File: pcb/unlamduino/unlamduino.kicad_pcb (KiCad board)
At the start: 2 copper layers, 41 parts, among them IC2 ATMEGA328-P, P3 CONN_01X08, U1 LM2576, U2 AP111733, Y2 16MHz

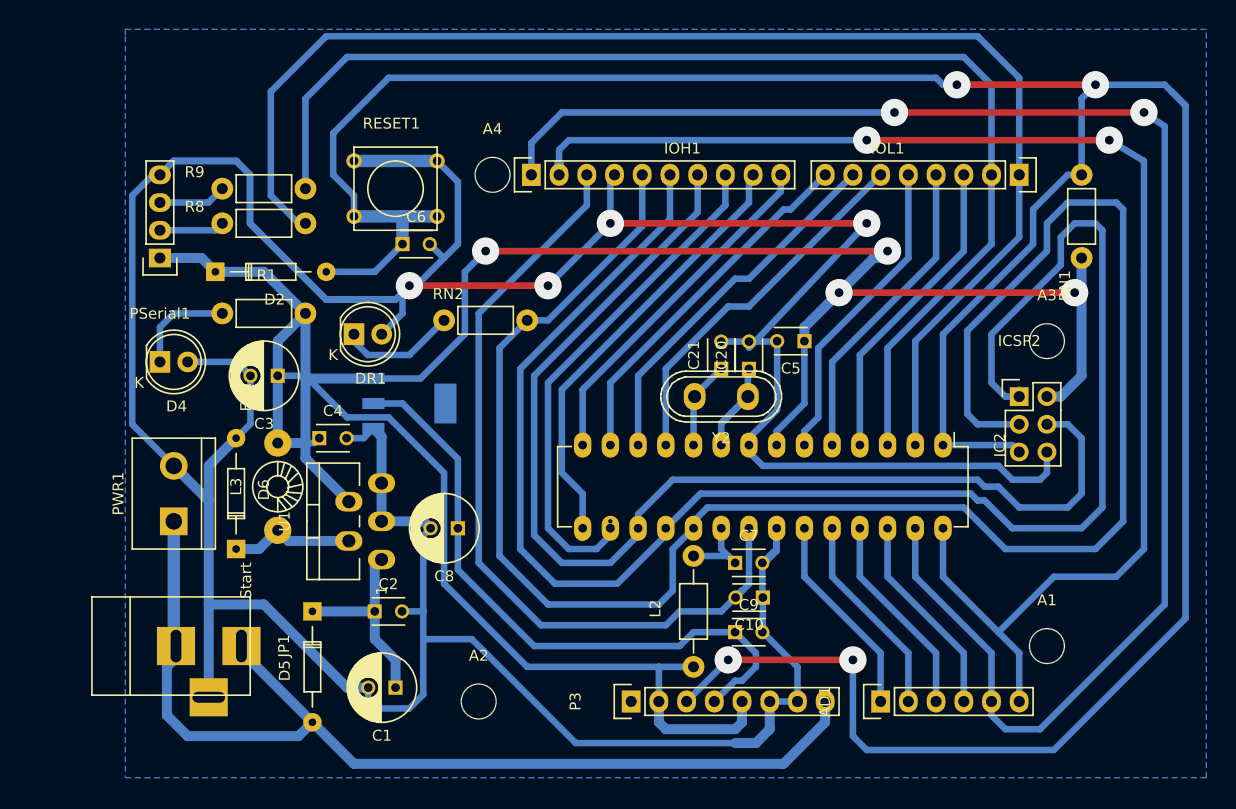
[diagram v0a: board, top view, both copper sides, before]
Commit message: Dibujo del borde de la placa.
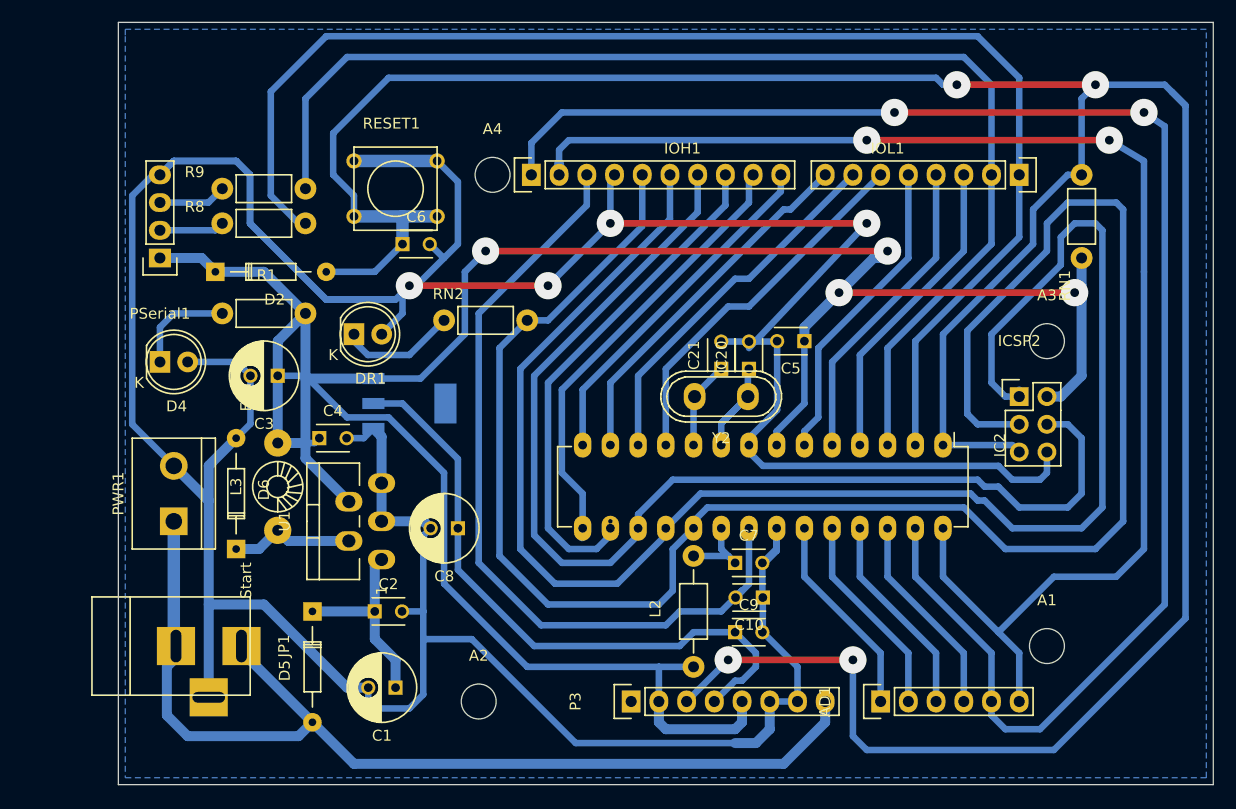
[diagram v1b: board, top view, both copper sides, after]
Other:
- board outline added: 100.3 x 69.8 mm
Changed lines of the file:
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@@
     (area 0 0 0 0)
     (thickness 1.6)
-    (drawings 2)
+    (drawings 6)
     (tracks 477)
     (zones 0)
@@
     (pad 1 np_thru_hole circle (at 0 0) (size 3.2 3.2) (drill 3.2) (layers *.Cu *.Mask F.SilkS))
   )
+  (gr_line (start 158.115 38.735) (end 158.115 108.585) (angle 90) (layer Edge.Cuts) (width 0.1))
+  (gr_line (start 258.445 38.735) (end 158.115 38.735) (angle 90) (layer Edge.Cuts) (width 0.1))
+  (gr_line (start 258.445 108.585) (end 258.445 38.735) (angle 90) (layer Edge.Cuts) (width 0.1))
+  (gr_line (start 158.115 108.585) (end 258.445 108.585) (angle 90) (layer Edge.Cuts) (width 0.1))
   (dimension 72 (width 0.3) (layer Cmts.User)
     (gr_text 72,000mm (at 142.65 76 270) (layer Cmts.User)

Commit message: Agregado de texto indicador de Montajes y diseño. Patas 1 de los integrados
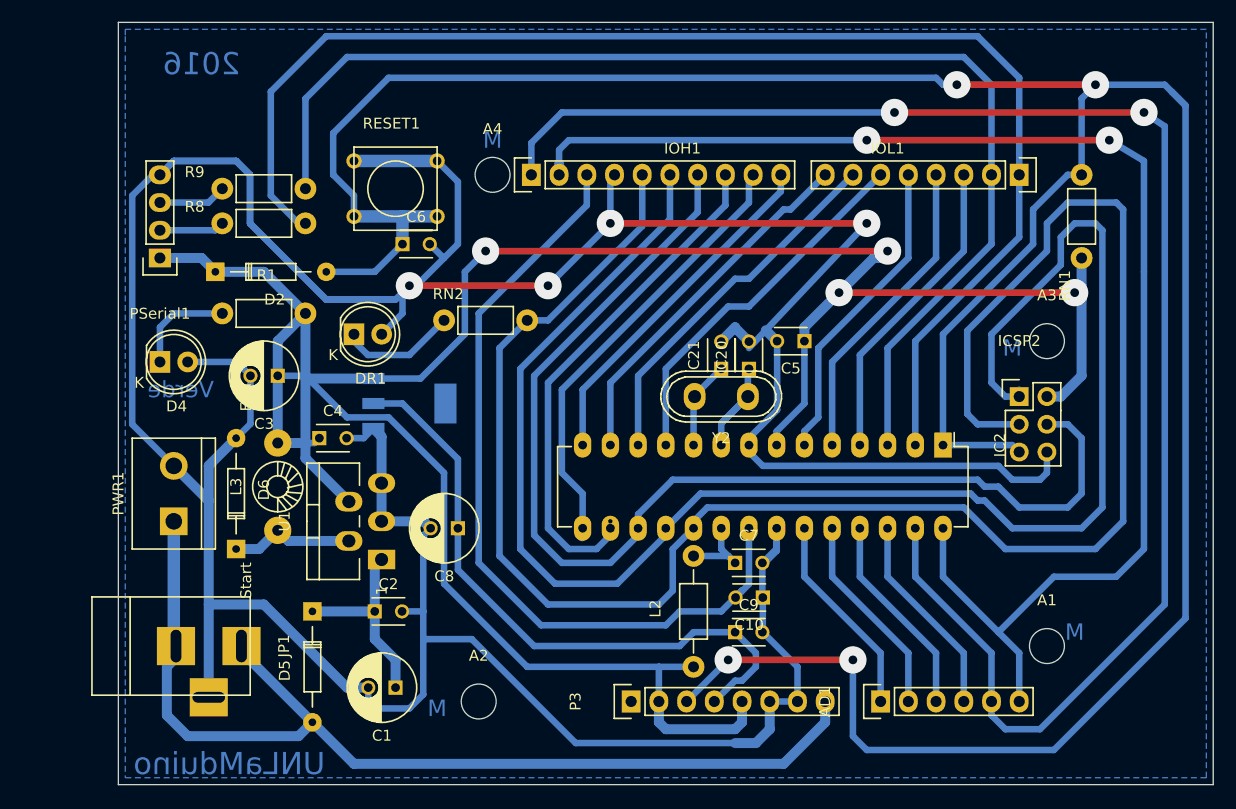
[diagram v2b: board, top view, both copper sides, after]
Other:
- board text added: "2016"
- board text added: "M"
- board text added: "UNLaMduino"
- board text added: "Verde"
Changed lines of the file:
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@@
     (links 101)
     (no_connects 0)
-    (area 0 0 0 0)
+    (area 136.57143 38.684999 264.000001 128.700001)
     (thickness 1.6)
-    (drawings 6)
-    (tracks 477)
+    (drawings 13)
+    (tracks 482)
     (zones 0)
     (modules 41)
@@
     (pad 3 thru_hole oval (at 0 3.79984 180) (size 2.49936 1.80086) (drill 1.19888) (layers *.Cu *.Mask F.SilkS)
       (net 7 GND))
-    (pad 1 thru_hole oval (at -3.50012 3.79984 180) (size 2.49936 1.80086) (drill 1.19888) (layers *.Cu *.Mask F.SilkS)
+    (pad 1 thru_hole rect (at -3.50012 3.79984 180) (size 2.49936 1.80086) (drill 1.19888) (layers *.Cu *.Mask F.SilkS)
       (net 8 "Net-(C1-Pad1)"))
     (pad 5 thru_hole oval (at 3.50012 3.79984 180) (size 2.49936 1.80086) (drill 1.19888) (layers *.Cu *.Mask F.SilkS)
@@
     (fp_line (start 0.135 35.315) (end 7.485 35.315) (layer F.SilkS) (width 0.15))
     (fp_line (start 0.135 -1.025) (end -1.15 -1.025) (layer F.SilkS) (width 0.15))
-    (pad 1 thru_hole oval (at 0 0 270) (size 2.3 1.6) (drill 0.8) (layers *.Cu *.Mask F.SilkS)
+    (pad 1 thru_hole rect (at 0 0 270) (size 2.3 1.6) (drill 0.8) (layers *.Cu *.Mask F.SilkS)
       (net 10 /RESET))
     (pad 2 thru_hole oval (at 0 2.54 270) (size 2.3 1.6) (drill 0.8) (layers *.Cu *.Mask F.SilkS)
@@
     (pad 1 np_thru_hole circle (at 0 0) (size 3.2 3.2) (drill 3.2) (layers *.Cu *.Mask F.SilkS))
   )
+  (gr_text "2016\n" (at 165.735 42.545) (layer B.Cu)
+    (effects (font (size 2.032 2.032) (thickness 0.381)) (justify mirror))
+  )
+  (gr_text UNLaMduino (at 168.275 106.68) (layer B.Cu)
+    (effects (font (size 2.032 2.032) (thickness 0.3556)) (justify mirror))
+  )
+  (gr_text Verde (at 163.83 72.39) (layer B.Cu)
+    (effects (font (size 1.5 1.5) (thickness 0.3)) (justify mirror))
+  )
+  (gr_text M (at 187.325 101.6) (layer B.Cu)
+    (effects (font (size 1.5 1.5) (thickness 0.3)) (justify mirror))
+  )
+  (gr_text M (at 192.405 49.53) (layer B.Cu)
+    (effects (font (size 1.5 1.5) (thickness 0.3)) (justify mirror))
+  )
+  (gr_text M (at 240.03 68.58) (layer B.Cu)
+    (effects (font (size 1.5 1.5) (thickness 0.3)) (justify mirror))
+  )
+  (gr_text M (at 245.745 94.615) (layer B.Cu)
+    (effects (font (size 1.5 1.5) (thickness 0.3)) (justify mirror))
+  )
   (gr_line (start 158.115 38.735) (end 158.115 108.585) (angle 90) (layer Edge.Cuts) (width 0.1))
   (gr_line (start 258.445 38.735) (end 158.115 38.735) (angle 90) (layer Edge.Cuts) (width 0.1))
@@
   (segment (start 238.76 94.615) (end 240.665 96.52) (width 0.6) (layer B.Cu) (net 6))
   (segment (start 198.501 52.705) (end 198.501 51.689) (width 0.9144) (layer B.Cu) (net 6) (status 30))
+  (segment (start 218.48 67.945) (end 218.44 67.945) (width 0.9144) (layer B.Cu) (net 7))
+  (segment (start 218.44 67.945) (end 217.442143 66.947143) (width 0.9144) (layer B.Cu) (net 7))
+  (segment (start 213.36 67.985) (end 213.36 67.945) (width 0.9144) (layer B.Cu) (net 7))
+  (segment (start 213.36 67.945) (end 214.63 66.675) (width 0.9144) (layer B.Cu) (net 7))
+  (segment (start 214.63 66.715) (end 215.9 67.985) (width 0.9144) (layer B.Cu) (net 7))
+  (segment (start 214.63 66.675) (end 214.63 66.715) (width 0.9144) (layer B.Cu) (net 7))
   (segment (start 182.23484 84.455) (end 186.095 84.455) (width 0.9144) (layer B.Cu) (net 7) (status 10))
   (segment (start 186.095 84.455) (end 186.73 85.09) (width 0.9144) (layer B.Cu) (net 7) (status 20))
@@
   (segment (start 240.03 80.645) (end 242.57 80.645) (width 0.6) (layer B.Cu) (net 7))
   (segment (start 238.76 79.375) (end 240.03 80.645) (width 0.6) (layer B.Cu) (net 7))
-  (segment (start 215.9 67.985) (end 218.44 67.985) (width 0.6) (layer B.Cu) (net 7) (status 30))
   (segment (start 218.44 67.985) (end 218.48 67.945) (width 0.6) (layer B.Cu) (net 7) (status 30))
-  (segment (start 213.36 67.985) (end 215.9 67.985) (width 0.6) (layer B.Cu) (net 7) (status 30))
   (segment (start 181.015 99.695) (end 181.015 101.005) (width 0.6) (layer B.Cu) (net 7) (status 10))
   (segment (start 184.785 101.6) (end 186.055 100.33) (width 0.6) (layer B.Cu) (net 7))
@@
   (segment (start 217.335002 88.265) (end 217.13 88.265) (width 0.6) (layer B.Cu) (net 7) (status 30))
   (segment (start 217.805 100.965) (end 217.805 101.6) (width 0.6) (layer B.Cu) (net 7) (status 30))
-  (segment (start 215.9 68.58) (end 226.695 57.15) (width 0.6) (layer B.Cu) (net 7) (status 10))
+  (segment (start 215.9 68.58) (end 217.442143 66.947143) (width 0.6) (layer B.Cu) (net 7) (status 10))
+  (segment (start 217.442143 66.947143) (end 226.695 57.15) (width 0.6) (layer B.Cu) (net 7) (status 10))
   (segment (start 203.2 57.15) (end 203.2 53.086) (width 0.6) (layer B.Cu) (net 7) (status 20))
   (via (at 203.2 57.15) (size 2.5) (drill 0.8) (layers F.Cu B.Cu) (net 7))

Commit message: Acomodado de serigrafía
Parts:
- moved IOH1 22.9 mm to (218.8, 52.7), turned to 270 degrees
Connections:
- IOH1 pad 1: /AD4/SDA -> /IO8
- IOH1 pad 10: /IO8 -> /AD4/SDA
- IOH1 pad 2: /AD5/SCL -> /IO9
- IOH1 pad 3: /AREF -> /IO10
- IOH1 pad 4: GND -> /IO11
- IOH1 pad 5: /IO13 -> /IO12
- IOH1 pad 6: /IO12 -> /IO13
- IOH1 pad 7: /IO11 -> GND
- IOH1 pad 8: /IO10 -> /AREF
- IOH1 pad 9: /IO9 -> /AD5/SCL
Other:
- board text added: "0"
- board text added: "Analog"

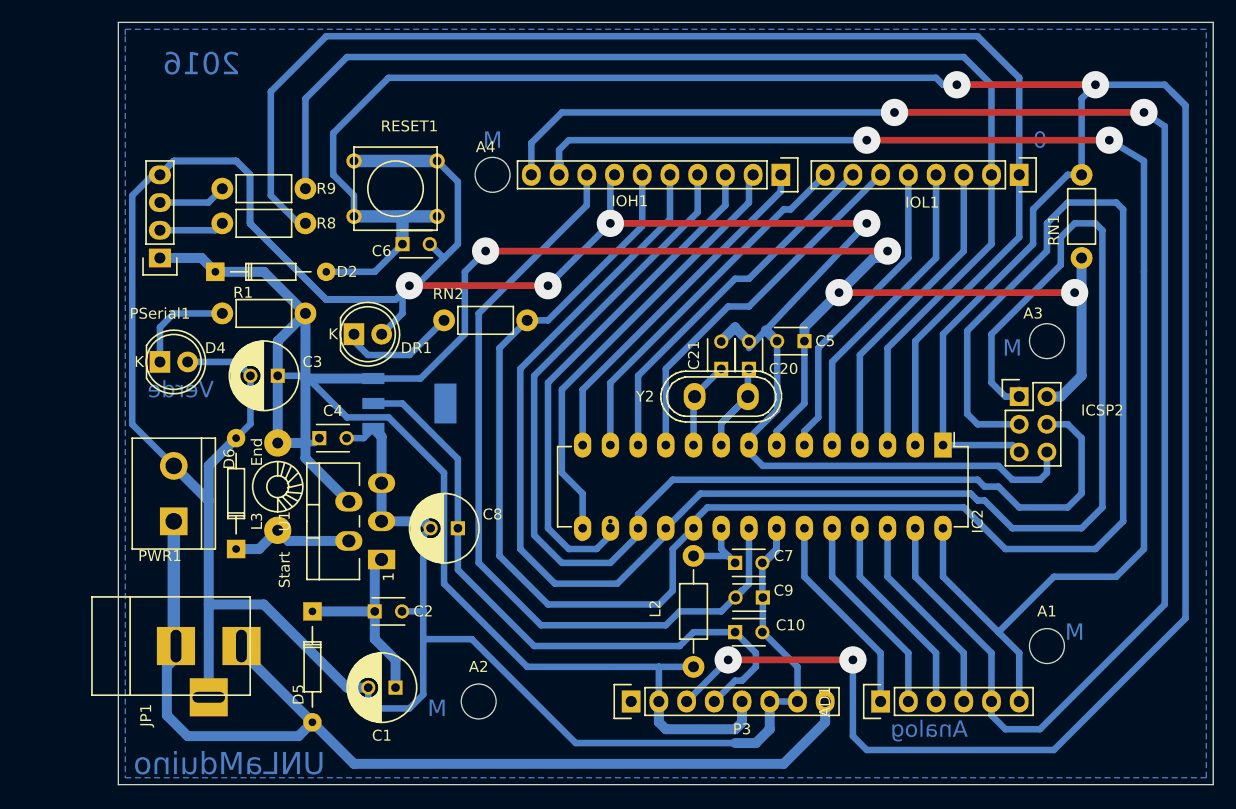
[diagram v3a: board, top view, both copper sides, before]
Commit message: Acomodado de algunos textos.
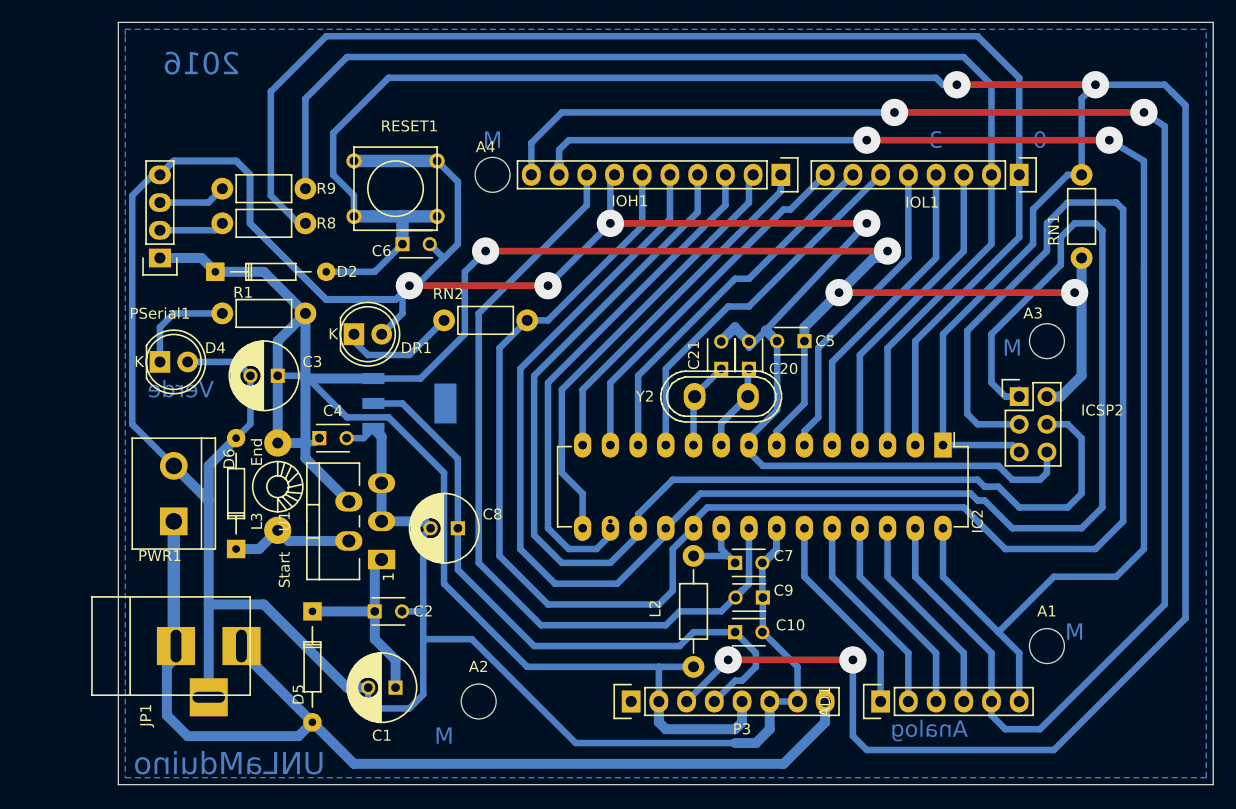
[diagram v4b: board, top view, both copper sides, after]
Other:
- board text added: "3"
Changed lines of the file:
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@@
     (area 158.064999 38.684999 258.495001 108.635001)
     (thickness 1.6)
-    (drawings 15)
+    (drawings 16)
     (tracks 482)
     (zones 0)
@@
       (effects (font (size 1 1) (thickness 0.15)))
     )
-    (fp_text value Agujero (at 0 4.2) (layer F.Fab)
+    (fp_text value Agujero (at 6.35 0) (layer F.Fab)
       (effects (font (size 1 1) (thickness 0.15)))
     )
@@
     (pad 1 np_thru_hole circle (at 0 0) (size 3.2 3.2) (drill 3.2) (layers *.Cu *.Mask F.SilkS))
   )
+  (gr_text 3 (at 233.045 49.53) (layer B.Cu)
+    (effects (font (size 1.5 1.5) (thickness 0.3)) (justify mirror))
+  )
   (gr_text "0\n" (at 242.57 49.53) (layer B.Cu)
     (effects (font (size 1.5 1.5) (thickness 0.3)) (justify mirror))
@@
     (effects (font (size 1.5 1.5) (thickness 0.3)) (justify mirror))
   )
-  (gr_text M (at 187.325 101.6) (layer B.Cu)
+  (gr_text M (at 187.96 104.14) (layer B.Cu)
     (effects (font (size 1.5 1.5) (thickness 0.3)) (justify mirror))
   )
